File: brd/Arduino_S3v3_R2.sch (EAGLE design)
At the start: 36 parts, among them J4 USB_B_PTH, U1 FT232RL, U2 ATMEGA328P_TQFP, U3 ADXL337, Y1 16MHz

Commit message: updated to SPI, replaced TH comps, new accel
New accelerometer is not hooked up yet.
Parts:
- removed C16, C17: 30p, rcl:C-USC0603
- removed Y1: 16MHz, SparkFun-Clocks:CRYSTAL-16MHZPTH-HC49US
- added AC2: LIS3DHTR, SamacSys_Parts:LIS3DHTR
- added Y2: CSTNE16M0V51Z000R0, SamacSys_Parts:CSTNE16M0V51Z000R0
- C5, C8: value 100u -> GRM31CR61A107ME05L; device rcl:CPOL-EUE3.5-8 -> SamacSys_Parts:GRM31CR61A107ME05L; MFR KEMET -> (none); MPN A750BK107M1AAAE024 -> (none)
- LCD: device pinhead:PINHD-1X4 -> pinhead:PINHD-1X6
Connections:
- removed net N$14: ICSP.1, LCD.1, U2.PC4(ADC4/SDA)
- removed net N$7: C16.1, U2.PB6(XTAL1/TOSC1), Y1.2
- new net LCD_CS: LCD.1, U2.PD2(INT0)
- new net LCD_SCL: LCD.4, U2.PD5(T1)
- new net LCD_SDA: LCD.3, U2.PD4(XCK/T0)
- new net LCD_SDO: LCD.2, U2.PD3(INT1)
- new net N$1: U2.PB6(XTAL1/TOSC1), Y2.INPUT_
- net +5V: now also C8.1, LCD.5; no longer C5.+, LCD.3
- net BUZZ: now also ICSP.1, U2.PC4(ADC4/SDA); no longer U2.ADC6
- net GND: now also C5.2, C8.2, LCD.6, Y2.GND_; no longer C16.2, C17.2, C5.-, C8.-, LCD.4
- net N$15: no longer LCD.2
- net N$6: now also Y2.OUT; no longer C17.1, Y1.1
- net VIN: now also C5.1; no longer C8.+
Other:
- moved on the sheet: C5, C7, C8, D1, IC1, LED14, LS1, R4, S1

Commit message: new accel, 3.3v regulator, final draft
Ready for Board Review.
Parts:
- removed U3: ADXL337, SparkFun-Sensors:ADXL337
- added C14: GRM31CR61A107ME05L, SamacSys_Parts:GRM31CR61A107ME05L
- added C15: 10uF, SparkFun-Capacitors:10UF-0603-6.3V-20%
- added IC2: LM1117IMP-3.3_NOPB, SamacSys_Parts:LM1117IMP-3.3_NOPB
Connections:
- net N$5 renamed VBUS
- removed net XOUT: JP1.3, U2.PC2(ADC2), U3.ZOUT
- removed net YOUT: JP1.2, U2.PC1(ADC1), U3.YOUT
- removed net ZOUT: JP1.1, U2.PC0(ADC0), U3.XOUT
- new net 3.3V: AC2.VDD, AC2.VDDIO, C15.1, IC2.VOUT
- new net ACC_SCL: AC2.SCL/SPC, JP1.1, U2.PB1(OC1A)
- new net ACC_SDA: AC2.SDA/SDI/SDO, JP1.2, U2.PB2(SS/OC1B)
- new net ACC_SDO: AC2.SDO/SA0, JP1.3, U2.PB3(MOSI/OC2)
- net +5V: now also C14.1, IC2.INPUT; no longer U3.VS@1, U3.VS@2
- net GND: now also AC2.CS, AC2.GND_1, AC2.GND_2, AC2.RES, C14.2, C15.2, IC2.ADJ/GND; no longer U3.GND@1, U3.GND@2, U3.ST
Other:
- note added: "3.3V Power"
- moved on the sheet: AC2, JP1, LCD

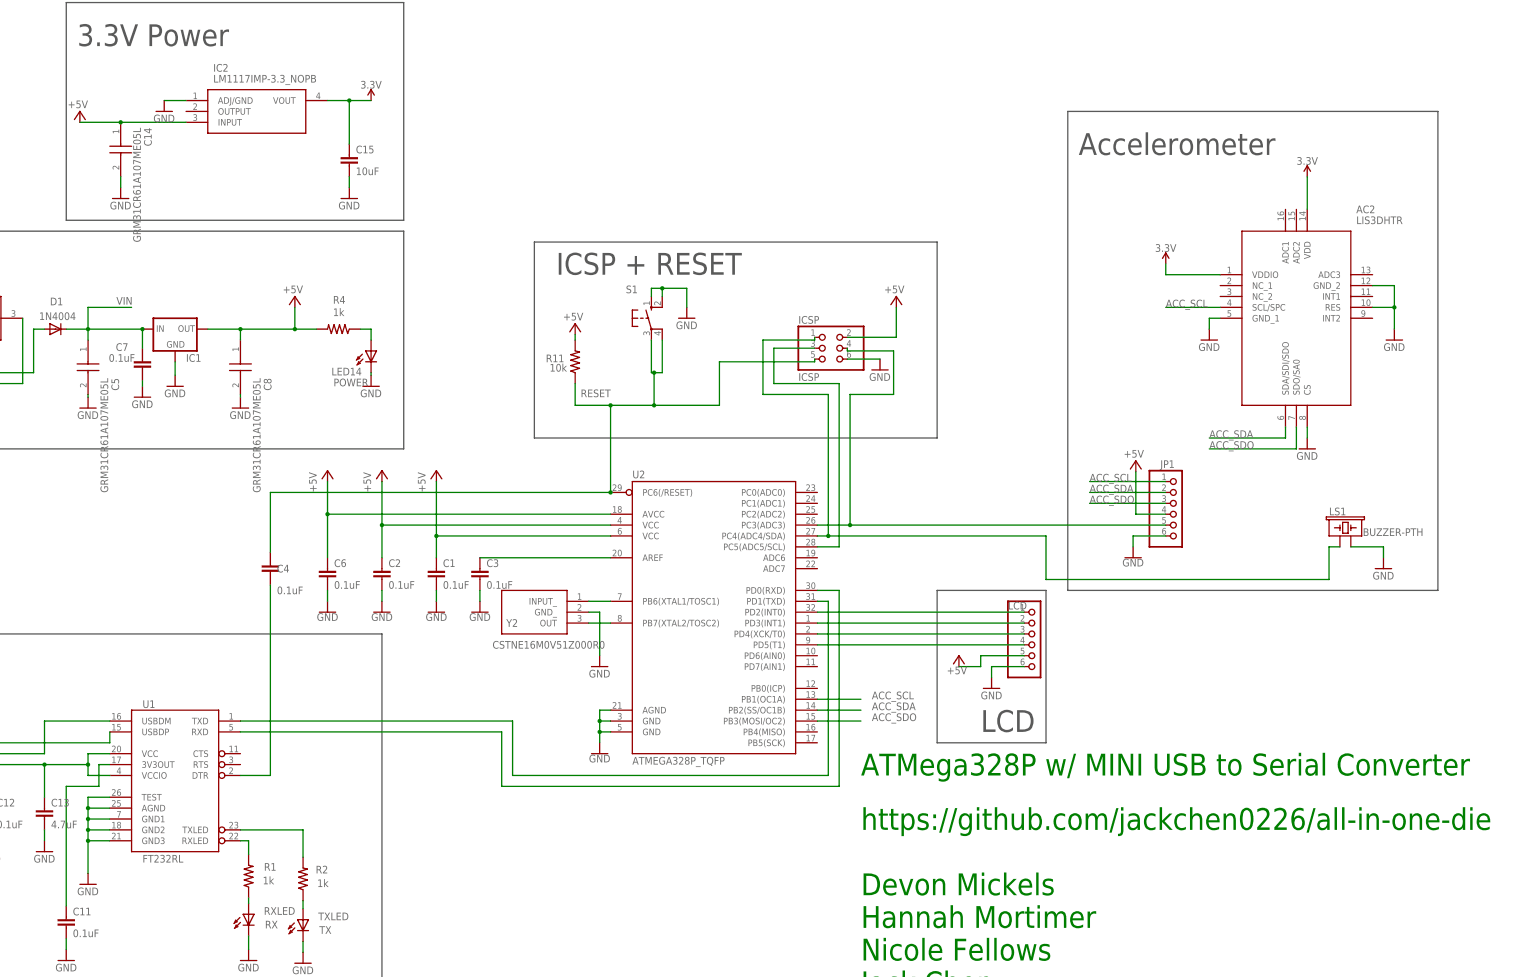
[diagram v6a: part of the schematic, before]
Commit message: Modified according to Desgin Review w/ Greenberg
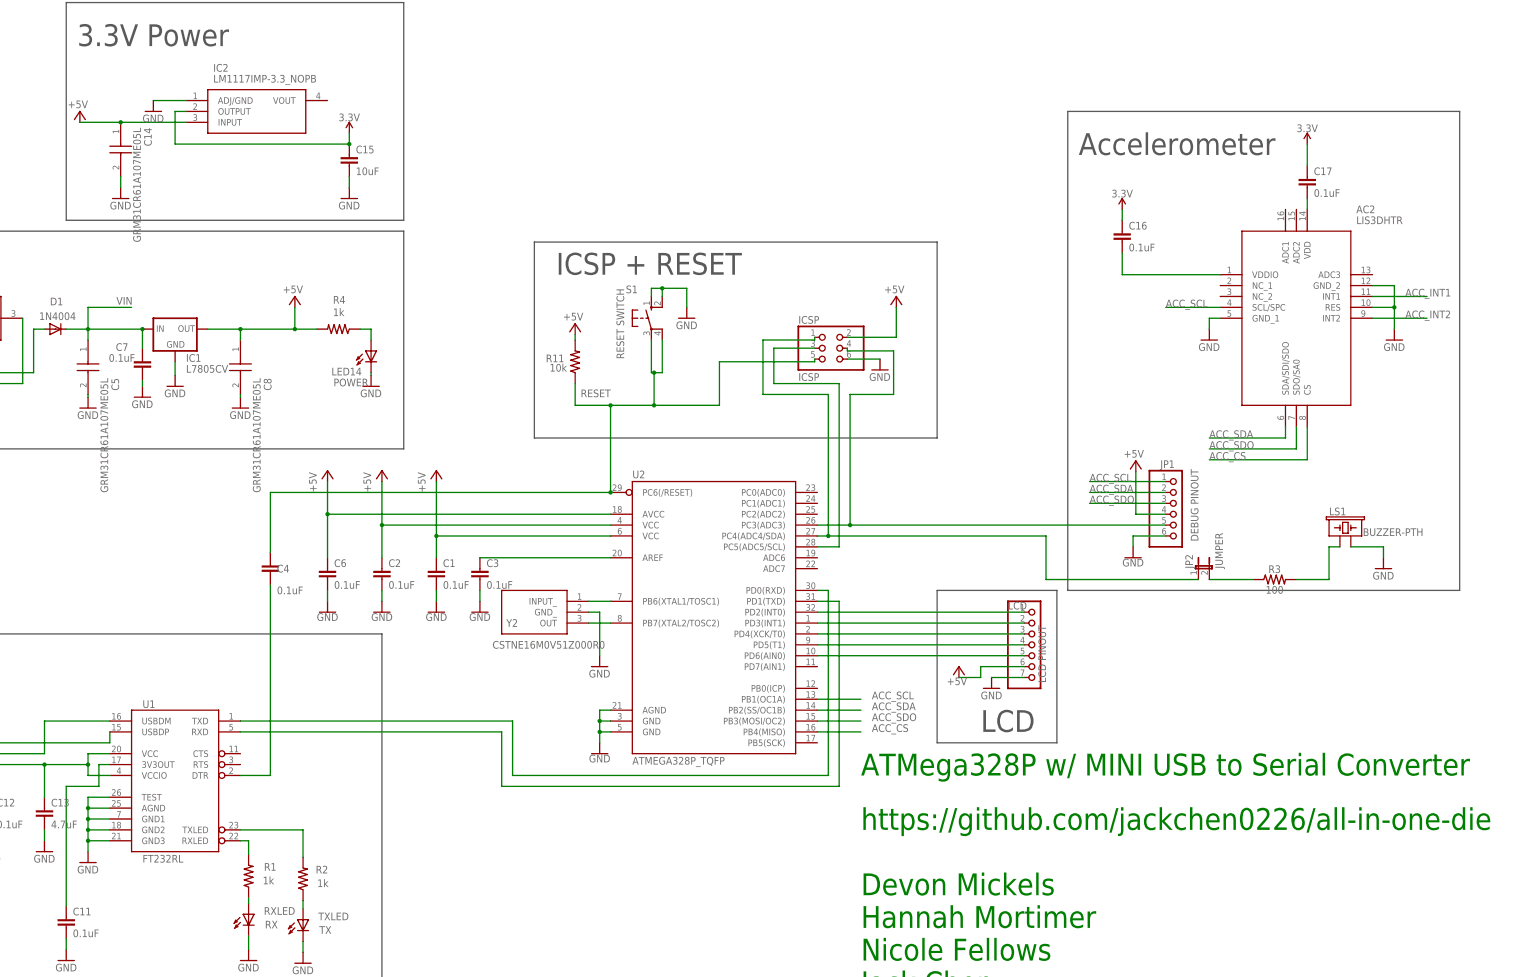
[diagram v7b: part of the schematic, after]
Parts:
- added C16, C17: 0.1uF, SparkFun-Capacitors:0.1UF-0603-25V-(+80/-20%)
- added JP2: JUMPER, jumper:JP1E
- added R3: 100, SparkFun-Resistors:100OHM-0603-1/4W-5%
- IC1: value (none) -> L7805CV
- JP1: value (none) -> DEBUG PINOUT
- LCD: value (none) -> LCD PINOUT; device pinhead:PINHD-1X6 -> pinhead:PINHD-1X7
- S1: value (none) -> RESET SWITCH
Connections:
- new net ACC_CS: AC2.CS, U2.PB4(MISO)
- new net ACC_INT1: AC2.INT1
- new net ACC_INT2: AC2.INT2
- new net N$11: LCD.5, U2.PD6(AIN0)
- new net N$12: JP2.2, R3.1
- new net N$14: LS1.1, R3.2
- new net N$5: AC2.VDD, C17.2
- new net N$7: AC2.VDDIO, C16.2
- net +5V: now also LCD.6; no longer LCD.5
- net 3.3V: now also C16.1, C17.1, IC2.OUTPUT; no longer AC2.VDD, AC2.VDDIO, IC2.VOUT
- net BUZZ: now also JP2.1; no longer LS1.1
- net GND: now also LCD.7; no longer AC2.CS, LCD.6
- net RXD: now also U2.PD1(TXD); no longer U2.PD0(RXD)
- net TXD: now also U2.PD0(RXD); no longer U2.PD1(TXD)

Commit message: Modified after meeting w/ Team 13
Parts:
- JP1: device adafruit:PINHD-1X6 -> pinhead:PINHD-1X7
- renumbered LED14 to PWR
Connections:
- net +5V: now also JP1.5; no longer JP1.4
- net ACC_CS: now also JP1.4
- net GND: now also JP1.7; no longer JP1.6
- net POTIN: now also JP1.6; no longer JP1.5
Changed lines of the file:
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@@
 </part>
 <part name="GND12" library="supply1" deviceset="GND" device=""/>
-<part name="LED14" library="led" deviceset="LED" device="3MM" value="POWER">
+<part name="PWR" library="led" deviceset="LED" device="3MM" value="POWER">
 <attribute name="MFR" value="VCC"/>
 <attribute name="MPN" value="LTH3MM12VFR4100"/>
@@
 <part name="GND3" library="supply1" library_urn="urn:adsk.eagle:library:371" deviceset="GND" device=""/>
 <part name="GND27" library="supply1" library_urn="urn:adsk.eagle:library:371" deviceset="GND" device=""/>
-<part name="JP1" library="adafruit" library_urn="urn:adsk.eagle:library:420" deviceset="PINHD-1X6" device="" package3d_urn="urn:adsk.eagle:package:6240711/1" value="DEBUG PINOUT"/>
+<part name="JP1" library="pinhead" library_urn="urn:adsk.eagle:library:325" deviceset="PINHD-1X7" device="" package3d_urn="urn:adsk.eagle:package:22477/2" value="DEBUG PINOUT"/>
 <part name="LS1" library="SparkFun-Electromechanical" library_urn="urn:adsk.eagle:library:516" deviceset="BUZZER" device="-PTH" package3d_urn="urn:adsk.eagle:package:38558/1">
 <attribute name="MFR" value="TDK"/>
@@
 <text x="284.48" y="193.04" size="5.08" layer="97">Accelerometer</text>
 <text x="261.62" y="58.42" size="5.08" layer="97">LCD</text>
-<wire x1="-35.56" y1="81.28" x2="121.92" y2="81.28" width="0.1524" layer="97"/>
-<wire x1="121.92" y1="81.28" x2="121.92" y2="-2.54" width="0.1524" layer="97"/>
-<wire x1="121.92" y1="-2.54" x2="-35.56" y2="-2.54" width="0.1524" layer="97"/>
+<wire x1="-35.56" y1="81.28" x2="116.84" y2="81.28" width="0.1524" layer="97"/>
+<wire x1="116.84" y1="81.28" x2="116.84" y2="-2.54" width="0.1524" layer="97"/>
+<wire x1="116.84" y1="-2.54" x2="-35.56" y2="-2.54" width="0.1524" layer="97"/>
 <wire x1="-35.56" y1="-2.54" x2="-35.56" y2="81.28" width="0.1524" layer="97"/>
 <wire x1="5.08" y1="175.26" x2="127" y2="175.26" width="0.1524" layer="97"/>
@@
 <attribute name="VALUE" x="190.5" y="152.4" size="1.778" layer="96"/>
 </instance>
-<instance part="LED14" gate="G$1" x="119.38" y="147.32" smashed="yes">
+<instance part="PWR" gate="G$1" x="119.38" y="147.32" smashed="yes">
 <attribute name="NAME" x="117.221" y="143.383" size="1.778" layer="95" rot="R180"/>
 <attribute name="VALUE" x="118.745" y="140.843" size="1.778" layer="96" rot="R180"/>
@@
 </instance>
 <instance part="C8" gate="G$1" x="88.9" y="149.86" smashed="yes" rot="R270">
-<attribute name="NAME" x="95.25" y="140.97" size="1.778" layer="95" rot="R270" align="center-left"/>
-<attribute name="VALUE" x="92.71" y="140.97" size="1.778" layer="96" rot="R270" align="center-left"/>
+<attribute name="NAME" x="95.25" y="143.51" size="1.778" layer="95" rot="R270" align="center-left"/>
+<attribute name="VALUE" x="92.71" y="143.51" size="1.778" layer="96" rot="R270" align="center-left"/>
 </instance>
 <instance part="C5" gate="G$1" x="53.34" y="149.86" smashed="yes" rot="R270">
-<attribute name="NAME" x="59.69" y="140.97" size="1.778" layer="95" rot="R270" align="center-left"/>
-<attribute name="VALUE" x="57.15" y="140.97" size="1.778" layer="96" rot="R270" align="center-left"/>
+<attribute name="NAME" x="59.69" y="143.51" size="1.778" layer="95" rot="R270" align="center-left"/>
+<attribute name="VALUE" x="57.15" y="143.51" size="1.778" layer="96" rot="R270" align="center-left"/>
 </instance>
 <instance part="AC2" gate="G$1" x="317.5" y="165.1" smashed="yes">
@@
 </segment>
 <segment>
-<pinref part="P+8" gate="1" pin="+5V"/>
-<pinref part="JP1" gate="A" pin="4"/>
-<wire x1="297.815" y1="119.126" x2="297.815" y2="109.22" width="0.1524" layer="91"/>
-<wire x1="297.815" y1="109.22" x2="304.8" y2="109.22" width="0.1524" layer="91"/>
-</segment>
-<segment>
 <pinref part="P+10" gate="1" pin="+5V"/>
 <pinref part="IC2" gate="G$1" pin="INPUT"/>
@@
 <wire x1="261.62" y1="73.66" x2="271.78" y2="73.66" width="0.1524" layer="91"/>
 </segment>
+<segment>
+<pinref part="JP1" gate="A" pin="5"/>
+<pinref part="P+8" gate="1" pin="+5V"/>
+<wire x1="304.8" y1="106.68" x2="297.815" y2="106.68" width="0.1524" layer="91"/>
+<wire x1="297.815" y1="106.68" x2="297.815" y2="119.126" width="0.1524" layer="91"/>
+</segment>
 </net>
 <net name="GND" class="0">
@@
 <segment>
 <wire x1="119.38" y1="142.24" x2="119.38" y2="141.605" width="0.1524" layer="91"/>
-<pinref part="LED14" gate="G$1" pin="C"/>
+<pinref part="PWR" gate="G$1" pin="C"/>
 <pinref part="GND11" gate="1" pin="GND"/>
 </segment>
@@
 </segment>
 <segment>
-<pinref part="GND28" gate="1" pin="GND"/>
-<pinref part="JP1" gate="A" pin="6"/>
-<wire x1="297.18" y1="101.6" x2="297.18" y2="104.14" width="0.1524" layer="91"/>
-<wire x1="297.18" y1="104.14" x2="304.8" y2="104.14" width="0.1524" layer="91"/>
-</segment>
-<segment>
 <pinref part="Y2" gate="G$1" pin="GND_"/>
 <pinref part="GND3" gate="1" pin="GND"/>
@@
 <pinref part="LCD" gate="A" pin="7"/>
 <wire x1="264.16" y1="71.12" x2="271.78" y2="71.12" width="0.1524" layer="91"/>
+</segment>
+<segment>
+<pinref part="GND28" gate="1" pin="GND"/>
+<pinref part="JP1" gate="A" pin="7"/>
+<wire x1="297.18" y1="101.6" x2="304.8" y2="101.6" width="0.1524" layer="91"/>
 </segment>
 </net>
@@
 <wire x1="119.38" y1="149.86" x2="119.38" y2="152.4" width="0.1524" layer="91"/>
 <pinref part="R4" gate="G$1" pin="1"/>
-<pinref part="LED14" gate="G$1" pin="A"/>
+<pinref part="PWR" gate="G$1" pin="A"/>
 </segment>
 </net>
@@
 <wire x1="231.14" y1="137.16" x2="231.14" y2="106.68" width="0.1524" layer="91"/>
 <wire x1="231.14" y1="106.68" x2="223.52" y2="106.68" width="0.1524" layer="91"/>
-<wire x1="231.14" y1="106.68" x2="304.8" y2="106.68" width="0.1524" layer="91"/>
+<wire x1="231.14" y1="106.68" x2="292.1" y2="106.68" width="0.1524" layer="91"/>
+<wire x1="292.1" y1="106.68" x2="292.1" y2="104.14" width="0.1524" layer="91"/>
 <junction x="231.14" y="106.68"/>
-<pinref part="JP1" gate="A" pin="5"/>
+<pinref part="JP1" gate="A" pin="6"/>
+<wire x1="292.1" y1="104.14" x2="304.8" y2="104.14" width="0.1524" layer="91"/>
 </segment>
 </net>
@@
 <label x="314.96" y="121.92" size="1.778" layer="95"/>
 </segment>
-</net>
+<segment>
+<pinref part="JP1" gate="A" pin="4"/>
+<wire x1="304.8" y1="109.22" x2="287.02" y2="109.22" width="0.1524" layer="91"/>
+<label x="287.02" y="109.22" size="1.778" layer="95"/>
+</segment>
+</net>
